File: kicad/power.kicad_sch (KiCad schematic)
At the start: 35 parts, among them J8 Jack-DC, SW1 SW_SPDT, U9 ICL7660

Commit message: Tweaking values now that build is in progress
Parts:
- removed J8: Jack-DC, KK254_Horizontal:Molex_KK-254_1x02_P2.54mm_Horizontal, symbol Connector:Jack-DC
- added J3: Conn_01x03_Pin, Rumblesan_Connectors:Molex_KK-254_22-05-7038_1x03_P2.54mm_Horizontal, symbol Connector:Conn_01x03_Pin
- added J8: Conn_01x02, Rumblesan_Connectors:Molex_KK-254_22-05-7028_1x02_P2.54mm_Horizontal, symbol Connector_Generic:Conn_01x02
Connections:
- net GND: now also J3.2 (Pin_2), J8.2 (Pin_2); no longer D3.2 (A)
- net VCC: now also D3.2 (A), J3.1 (Pin_1); no longer D3.1 (K), SW1.1 (A)
- net VEE: now also J3.3 (Pin_3)
- net at SW1.2 (B): now also J8.1 (Pin_1)
- new net: D3.1 (K), SW1.1 (A)
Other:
- note added: "Power"
- moved on the sheet: D3, NT1, SW1

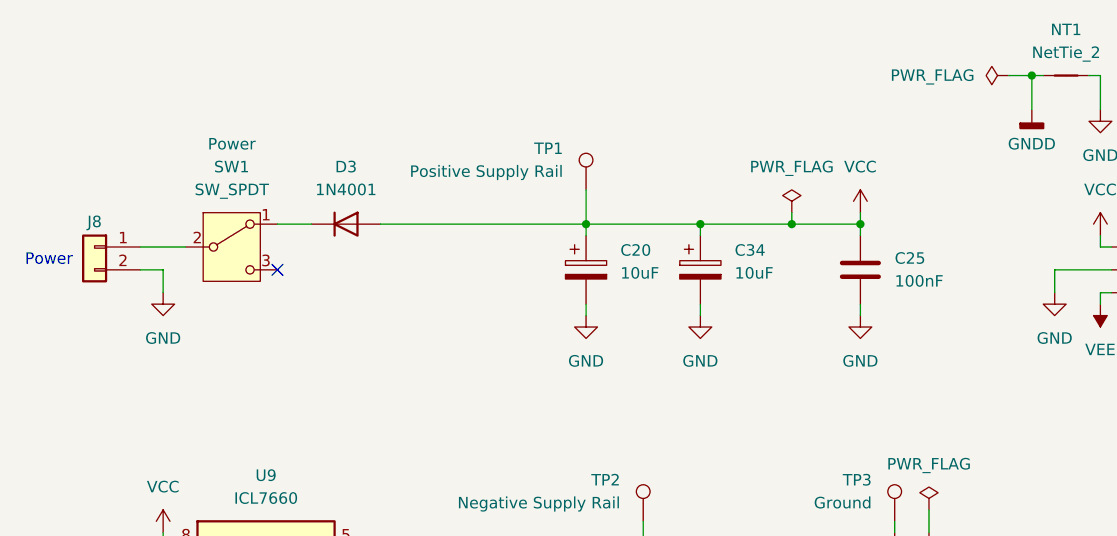
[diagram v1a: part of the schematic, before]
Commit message: Fixing issues with power circuitry
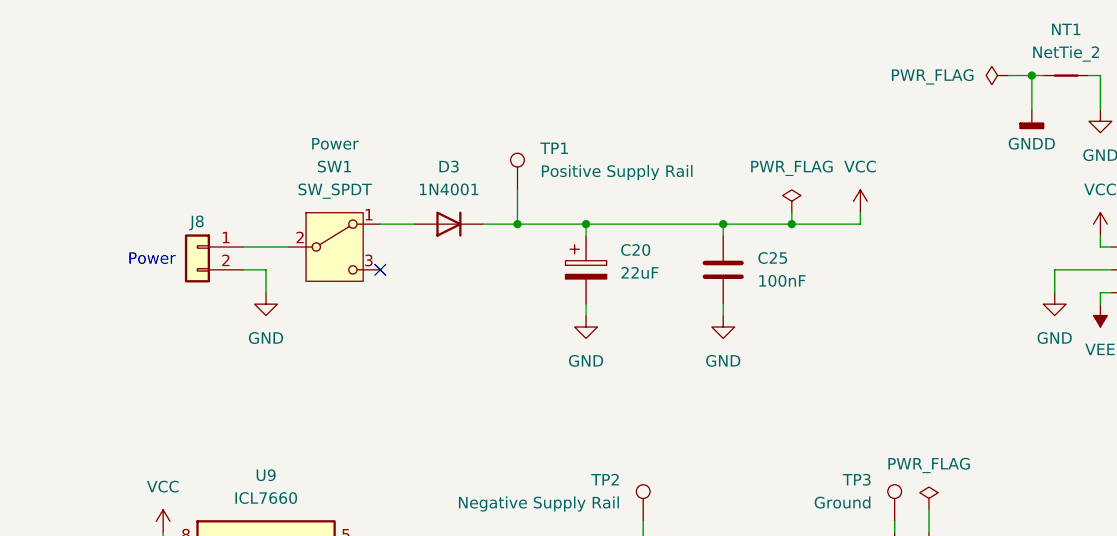
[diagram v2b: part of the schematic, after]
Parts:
- removed C34: 10uF, Rumblesan_Standard_Parts:CP_Radial_D5.0mm_P2.00mm, symbol Rumblesan_Standard_Parts:C_Polarized
- C20: value 10uF -> 22uF
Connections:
- net VCC: now also D3.1 (K); no longer D3.2 (A)
- net at SW1.1 (A): now also D3.2 (A); no longer D3.1 (K)
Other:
- moved on the sheet: C25, D3, J8, SW1, TP1

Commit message: Tweaking PCB
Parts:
- added C42, C43: 10uF, Rumblesan_Standard_Parts:CP_Radial_D5.0mm_P2.00mm, symbol Rumblesan_Standard_Parts:C_Polarized
- added D6, D7: 5v1, Diode_THT:D_DO-41_SOD81_P10.16mm_Horizontal, symbol Device:D_Zener
- added R26, R27: 1k, Rumblesan_Standard_Parts:R_Axial_DIN0207_L6.3mm_D2.5mm_P10.16mm_Horizontal, symbol Rumblesan_Standard_Parts:R
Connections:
- net GND: now also C42.2, C43.1, D6.2 (A), D7.1 (K)
- net VCC: now also R26.1
- net VEE: now also R27.1
- new net NEG_5V_REF: C43.2, D7.2 (A), R27.2
- new net POS_5V_REF: C42.1, D6.1 (K), R26.2

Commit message: More pcb tweaks
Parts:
- J8: Name (none) -> Power Input
- TP1: Name (none) -> +V
- TP2: Name (none) -> -V
- TP3: Name (none) -> 0V
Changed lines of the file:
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@@
 			)
 		)
+		(property "Name" "+V"
+			(at 88.9 41.91 0)
+			(effects
+				(font
+					(size 1.27 1.27)
+				)
+				(hide yes)
+			)
+		)
 		(pin "1"
 		)
@@
 			)
 		)
+		(property "Name" "0V"
+			(at 130.81 78.74 0)
+			(effects
+				(font
+					(size 1.27 1.27)
+				)
+				(hide yes)
+			)
+		)
 		(pin "1"
 		)
@@
 			)
 		)
+		(property "Name" "Power Input"
+			(at 53.34 48.26 0)
+			(effects
+				(font
+					(size 1.27 1.27)
+				)
+				(hide yes)
+			)
+		)
 		(pin "1"
 		)
@@
 			(at 102.87 78.74 0)
 			(effects
+				(font
+					(size 1.27 1.27)
+				)
+				(hide yes)
+			)
+		)
+		(property "Name" "-V"
+			(at 102.87 78.74 0)
+			(effects
